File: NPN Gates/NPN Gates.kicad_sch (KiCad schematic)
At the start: 63 parts, among them J1 Conn_01x02, Q1 BC547, Q10 BC547, Q11 BC547, Q12 BC547, Q13 BC547, Q14 BC547, Q15 BC547, Q16 BC547, Q17 BC547, Q18 BC547, Q19 BC547, Q2 BC547, Q20 BC547, Q21 BC547, Q22 BC547, Q23 BC547, Q24 BC547, Q3 BC547, Q4 BC547, Q5 BC547, Q6 BC547, Q7 BC547, Q8 BC547, Q9 BC547, SW1 A, SW2 B

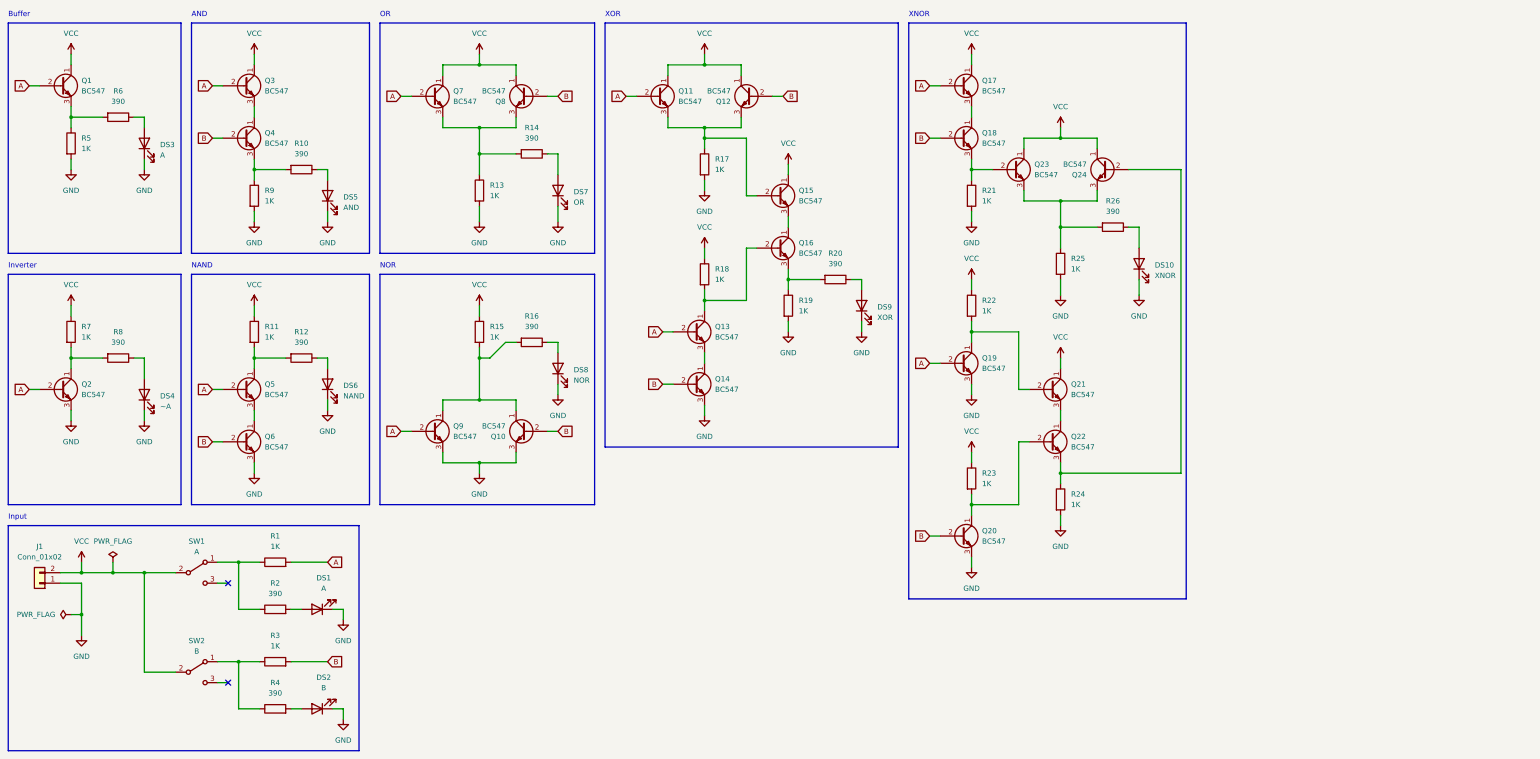
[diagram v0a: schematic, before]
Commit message: chore: Using D for LEDs instead of DS
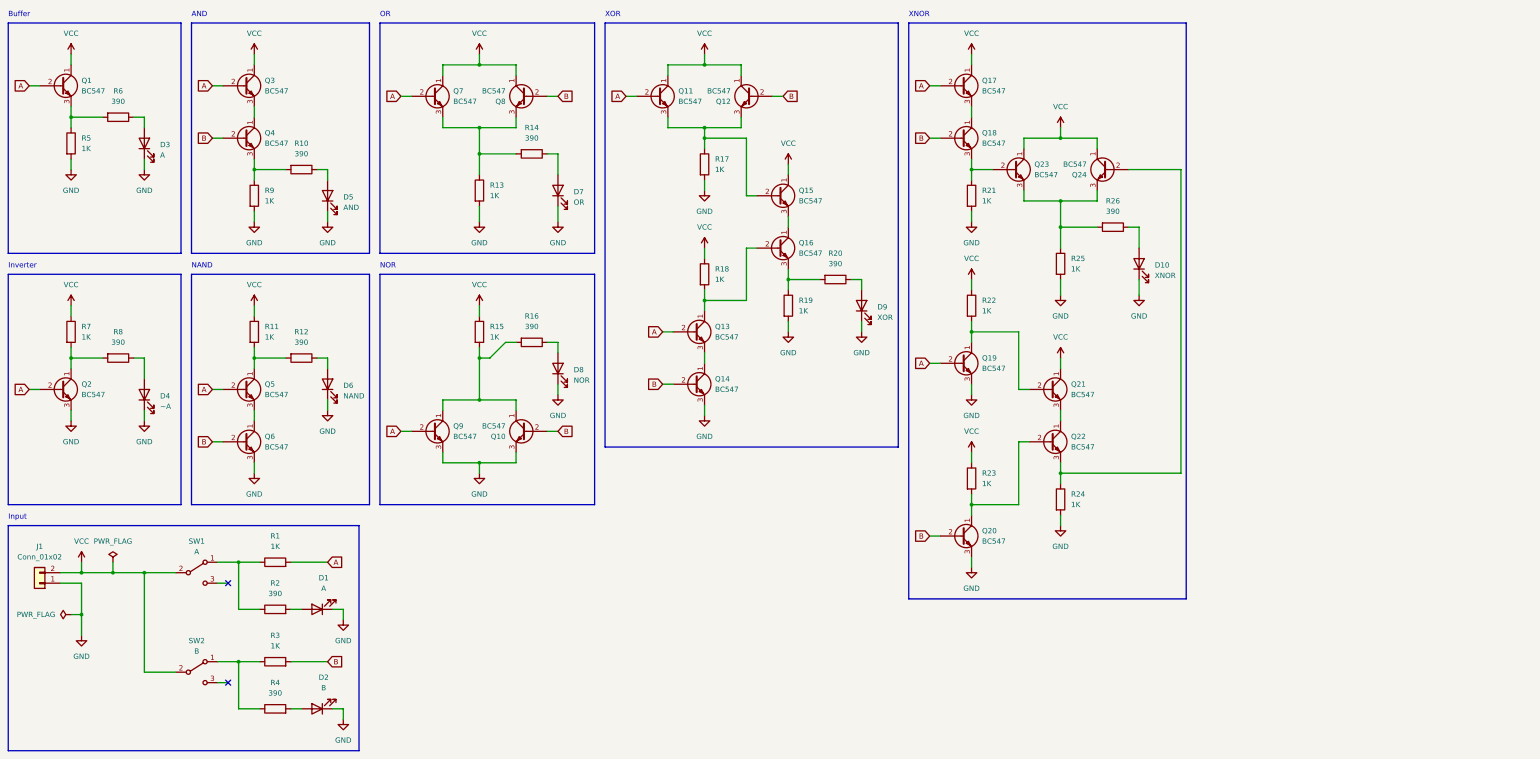
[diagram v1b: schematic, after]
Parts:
- renumbered DS1 to D1, DS10 to D10, DS2 to D2, DS3 to D3, DS4 to D4, DS5 to D5, DS6 to D6, DS7 to D7, DS8 to D8, DS9 to D9
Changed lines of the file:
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@@
   (symbol (lib_id "Device:LED") (at 48.26 107.95 90) (unit 1)
     (in_bom yes) (on_board yes) (dnp no) (fields_autoplaced)
-    (property "Reference" "DS4" (at 52.07 108.2675 90)
+    (property "Reference" "D4" (at 52.07 108.2675 90)
       (effects (font (size 1.27 1.27)) (justify right))
     )
@@
       (project "NPN Gates"
         (path "/9a54ea90-4d84-4fa4-90d3-d802e15aa898"
-          (reference "DS4") (unit 1)
+          (reference "D4") (unit 1)
         )
       )
@@
   (symbol (lib_id "Device:LED") (at 92.71 59.69 90) (unit 1)
     (in_bom yes) (on_board yes) (dnp no) (fields_autoplaced)
-    (property "Reference" "DS5" (at 96.52 60.0075 90)
+    (property "Reference" "D5" (at 96.52 60.0075 90)
       (effects (font (size 1.27 1.27)) (justify right))
     )
@@
       (project "NPN Gates"
         (path "/9a54ea90-4d84-4fa4-90d3-d802e15aa898"
-          (reference "DS5") (unit 1)
+          (reference "D5") (unit 1)
         )
       )
@@
   (symbol (lib_id "Device:LED") (at 148.59 58.42 90) (unit 1)
     (in_bom yes) (on_board yes) (dnp no) (fields_autoplaced)
-    (property "Reference" "DS7" (at 152.4 58.7375 90)
+    (property "Reference" "D7" (at 152.4 58.7375 90)
       (effects (font (size 1.27 1.27)) (justify right))
     )
@@
       (project "NPN Gates"
         (path "/9a54ea90-4d84-4fa4-90d3-d802e15aa898"
-          (reference "DS7") (unit 1)
+          (reference "D7") (unit 1)
         )
       )
@@
   (symbol (lib_id "Device:LED") (at 92.71 105.41 90) (unit 1)
     (in_bom yes) (on_board yes) (dnp no) (fields_autoplaced)
-    (property "Reference" "DS6" (at 96.52 105.7275 90)
+    (property "Reference" "D6" (at 96.52 105.7275 90)
       (effects (font (size 1.27 1.27)) (justify right))
     )
@@
       (project "NPN Gates"
         (path "/9a54ea90-4d84-4fa4-90d3-d802e15aa898"
-          (reference "DS6") (unit 1)
+          (reference "D6") (unit 1)
         )
       )
@@
   (symbol (lib_id "Device:LED") (at 148.59 101.6 90) (unit 1)
     (in_bom yes) (on_board yes) (dnp no) (fields_autoplaced)
-    (property "Reference" "DS8" (at 152.4 101.9175 90)
+    (property "Reference" "D8" (at 152.4 101.9175 90)
       (effects (font (size 1.27 1.27)) (justify right))
     )
@@
       (project "NPN Gates"
         (path "/9a54ea90-4d84-4fa4-90d3-d802e15aa898"
-          (reference "DS8") (unit 1)
+          (reference "D8") (unit 1)
         )
       )
@@
   (symbol (lib_id "Device:LED") (at 289.56 76.2 90) (unit 1)
     (in_bom yes) (on_board yes) (dnp no) (fields_autoplaced)
-    (property "Reference" "DS10" (at 293.37 76.5175 90)
+    (property "Reference" "D10" (at 293.37 76.5175 90)
       (effects (font (size 1.27 1.27)) (justify right))
     )
@@
       (project "NPN Gates"
         (path "/9a54ea90-4d84-4fa4-90d3-d802e15aa898"
-          (reference "DS10") (unit 1)
+          (reference "D10") (unit 1)
         )
       )
@@
   (symbol (lib_id "Device:LED") (at 90.17 160.02 180) (unit 1)
     (in_bom yes) (on_board yes) (dnp no) (fields_autoplaced)
-    (property "Reference" "DS1" (at 91.7575 152.4 0)
+    (property "Reference" "D1" (at 91.7575 152.4 0)
       (effects (font (size 1.27 1.27)))
     )
@@
       (project "NPN Gates"
         (path "/9a54ea90-4d84-4fa4-90d3-d802e15aa898"
-          (reference "DS1") (unit 1)
+          (reference "D1") (unit 1)
         )
       )
@@
   (symbol (lib_id "Device:LED") (at 90.17 184.15 180) (unit 1)
     (in_bom yes) (on_board yes) (dnp no) (fields_autoplaced)
-    (property "Reference" "DS2" (at 91.7575 176.53 0)
+    (property "Reference" "D2" (at 91.7575 176.53 0)
       (effects (font (size 1.27 1.27)))
     )
@@
       (project "NPN Gates"
         (path "/9a54ea90-4d84-4fa4-90d3-d802e15aa898"
-          (reference "DS2") (unit 1)
+          (reference "D2") (unit 1)
         )
       )
@@
   (symbol (lib_id "Device:LED") (at 222.25 86.36 90) (unit 1)
     (in_bom yes) (on_board yes) (dnp no) (fields_autoplaced)
-    (property "Reference" "DS9" (at 226.06 86.6775 90)
+    (property "Reference" "D9" (at 226.06 86.6775 90)
       (effects (font (size 1.27 1.27)) (justify right))
     )
@@
       (project "NPN Gates"
         (path "/9a54ea90-4d84-4fa4-90d3-d802e15aa898"
-          (reference "DS9") (unit 1)
+          (reference "D9") (unit 1)
         )
       )
@@
   (symbol (lib_id "Device:LED") (at 48.26 46.99 90) (unit 1)
     (in_bom yes) (on_board yes) (dnp no) (fields_autoplaced)
-    (property "Reference" "DS3" (at 52.07 47.3075 90)
+    (property "Reference" "D3" (at 52.07 47.3075 90)
       (effects (font (size 1.27 1.27)) (justify right))
     )
@@
       (project "NPN Gates"
         (path "/9a54ea90-4d84-4fa4-90d3-d802e15aa898"
-          (reference "DS3") (unit 1)
-        )
-      )
+          (reference "D3") (unit 1)
+        )
+      )

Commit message: fix: Fixed the NPN Gates project with a new design
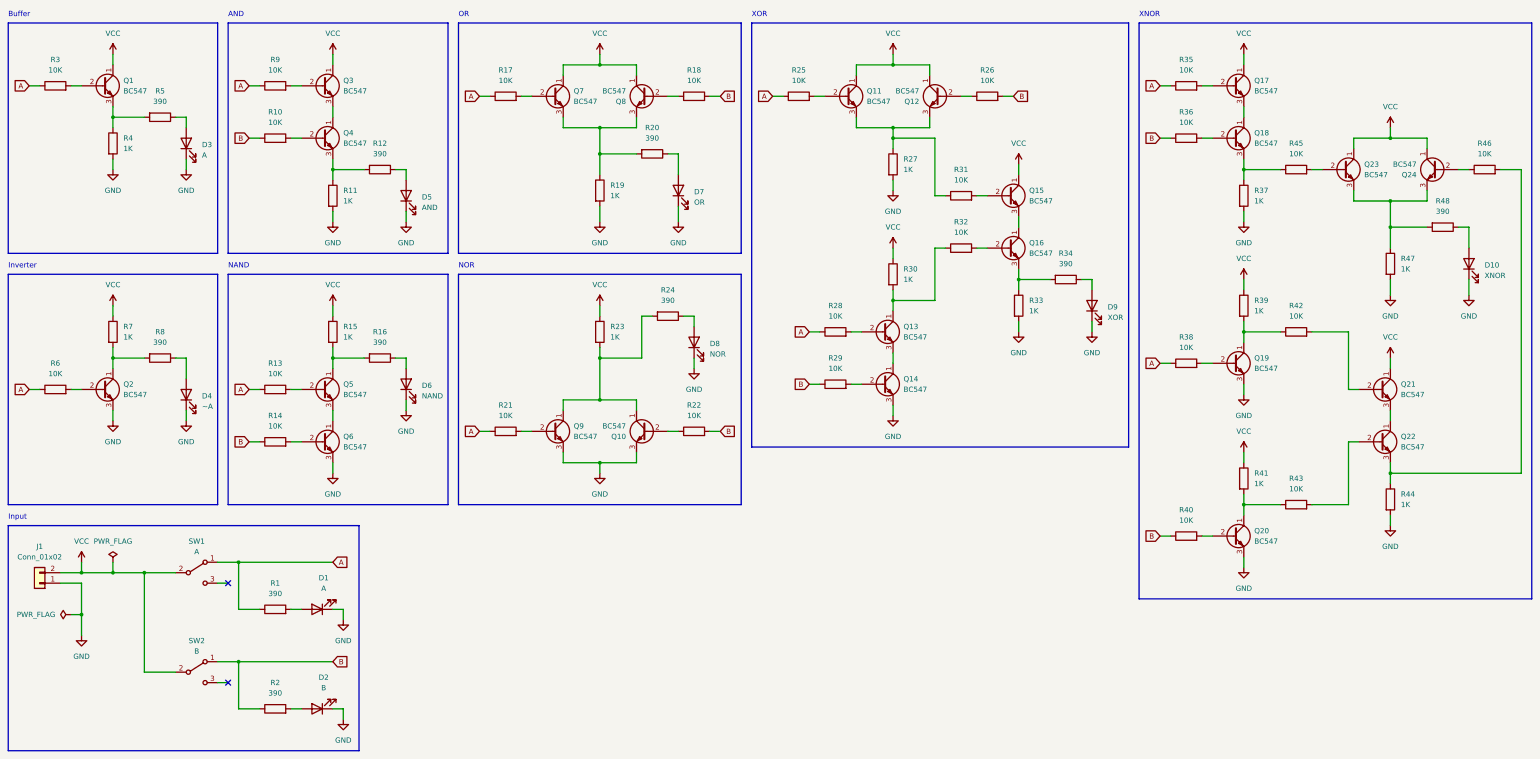
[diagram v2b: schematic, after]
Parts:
- removed R1: 1K, XS:Resistor-Vishay-CCF07, symbol Device:R
- added R10, R13, R14, R17, R18, R21, R22, R25, R26, R28, R29, R31, R32, R35, R36, R38, R40, R42, R43, R45, R46, R6, R9: 10K, XS:Resistor-Vishay-CCF07, symbol Device:R
- R3: value 1K -> 10K
- renumbered R2 to R1, R9 to R11, R10 to R12, R11 to R15, R12 to R16, R13 to R19, R4 to R2, R14 to R20, R15 to R23, R16 to R24, R17 to R27, R18 to R30, R19 to R33, R20 to R34, R21 to R37, R22 to R39, R5 to R4, R23 to R41, R24 to R44, R25 to R47, R26 to R48, R6 to R5
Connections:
- net A: now also R1.1, R3.1, SW1.1 (A), R13.1, R17.1, R21.1, R25.1, R28.1, R35.1, R38.1, R6.1, R9.1; no longer Q1.2 (B), Q11.2 (B), Q13.2 (B), Q17.2 (B), Q19.2 (B), Q2.2 (B), Q3.2 (B), Q5.2 (B), Q7.2 (B), Q9.2 (B)
- net B: now also R2.1, SW2.1 (A), R10.1, R14.1, R18.2, R22.2, R26.2, R29.1, R36.1, R40.1; no longer Q10.2 (B), Q12.2 (B), Q14.2 (B), Q18.2 (B), Q20.2 (B), Q4.2 (B), Q6.2 (B), Q8.2 (B), R3.2
- net at Q19.1 (C), R39.2: now also R42.1; no longer Q21.2 (B)
- net at Q20.1 (C), R41.2: now also R43.1; no longer Q22.2 (B)
- net at Q22.3 (E), R44.1: now also R46.2; no longer Q24.2 (B)
- net at Q11.3 (E), Q12.3 (E), R27.1: now also R31.1; no longer Q15.2 (B)
- net at Q18.3 (E), R37.1: now also R45.1; no longer Q23.2 (B)
- net at Q13.1 (C), R30.2: now also R32.1; no longer Q16.2 (B)
- new net: Q6.2 (B), R14.2
- new net: Q2.2 (B), R6.2
- new net: Q19.2 (B), R38.2
- new net: Q7.2 (B), R17.2
- new net: Q14.2 (B), R29.2
- new net: Q20.2 (B), R40.2
- new net: Q22.2 (B), R43.2
- new net: Q1.2 (B), R3.2
- new net: Q11.2 (B), R25.2
- new net: Q8.2 (B), R18.1
- new net: Q15.2 (B), R31.2
- new net: Q23.2 (B), R45.2
- new net: Q21.2 (B), R42.2
- new net: Q9.2 (B), R21.2
- new net: Q16.2 (B), R32.2
- new net: Q5.2 (B), R13.2
- new net: Q13.2 (B), R28.2
- new net: Q3.2 (B), R9.2
- new net: Q4.2 (B), R10.2
- new net: Q18.2 (B), R36.2
- new net: Q10.2 (B), R22.1
- new net: Q17.2 (B), R35.2
- new net: Q24.2 (B), R46.1
- new net: Q12.2 (B), R26.1
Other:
- moved on the sheet: D10, D3, D4, D5, D6, D7, D8, D9, Q1, Q10, Q11, Q12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
